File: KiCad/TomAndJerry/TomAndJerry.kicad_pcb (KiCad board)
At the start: 2 copper layers, 1 part

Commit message: Second Test Upload
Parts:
- added REF**: CP_EIA-2012-12_Kemet-R, Capacitor_Tantalum_SMD:CP_EIA-2012-12_Kemet-R, F.Cu at (180.3, 55.9)
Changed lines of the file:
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@@
   )
   (net 0 "")
+  (footprint "Capacitor_Tantalum_SMD:CP_EIA-2012-12_Kemet-R" (layer "F.Cu")
+    (at 180.34 55.88)
+    (descr "Tantalum Capacitor SMD Kemet-R (2012-12 Metric), IPC_7351 nominal, (Body size from: https://www.vishay.com/docs/40182/tmch.pdf), generated with kicad-footprint-generator")
+    (tags "capacitor tantalum")
+    (attr smd)
+    (fp_text reference "REF**" (at 0 -1.58) (layer "F.SilkS")
+      (effects (font (size 1 1) (thickness 0.15)))
+    )
+    (fp_text value "CP_EIA-2012-12_Kemet-R" (at 0 1.58) (layer "F.Fab")
+      (effects (font (size 1 1) (thickness 0.15)))
+    )
+    (fp_text user "${REFERENCE}" (at 0 0) (layer "F.Fab")
+      (effects (font (size 0.5 0.5) (thickness 0.08)))
+    )
+    (fp_line (start -1.71 0.785) (end 1 0.785) (layer "F.SilkS") (width 0.12))
+    (fp_line (start -1.71 -0.785) (end -1.71 0.785) (layer "F.SilkS") (width 0.12))
+    (fp_line (start 1 -0.785) (end -1.71 -0.785) (layer "F.SilkS") (width 0.12))
+    (fp_line (start 1.7 -0.88) (end 1.7 0.88) (layer "F.CrtYd") (width 0.05))
+    (fp_line (start 1.7 0.88) (end -1.7 0.88) (layer "F.CrtYd") (width 0.05))
+    (fp_line (start -1.7 -0.88) (end 1.7 -0.88) (layer "F.CrtYd") (width 0.05))
+    (fp_line (start -1.7 0.88) (end -1.7 -0.88) (layer "F.CrtYd") (width 0.05))
+    (fp_line (start -0.6875 -0.625) (end -1 -0.3125) (layer "F.Fab") (width 0.1))
+    (fp_line (start -1 0.625) (end 1 0.625) (layer "F.Fab") (width 0.1))
+    (fp_line (start 1 0.625) (end 1 -0.625) (layer "F.Fab") (width 0.1))
+    (fp_line (start -1 -0.3125) (end -1 0.625) (layer "F.Fab") (width 0.1))
+    (fp_line (start 1 -0.625) (end -0.6875 -0.625) (layer "F.Fab") (width 0.1))
+    (pad "1" smd roundrect (at -0.8875 0) (size 1.125 1.05) (layers "F.Cu" "F.Paste" "F.Mask") (roundrect_rratio 0.238095))
+    (pad "2" smd roundrect (at 0.8875 0) (size 1.125 1.05) (layers "F.Cu" "F.Paste" "F.Mask") (roundrect_rratio 0.238095))
+    (model "${KICAD6_3DMODEL_DIR}/Capacitor_Tantalum_SMD.3dshapes/CP_EIA-2012-12_Kemet-R.wrl"
+      (offset (xyz 0 0 0))
+      (scale (xyz 1 1 1))
+      (rotate (xyz 0 0 0))
+    )
+  )
   (footprint "Capacitor_Tantalum_SMD:CP_EIA-1608-08_AVX-J" (layer "F.Cu")
     (at 241.3 55.88)

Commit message: 3rd test upload
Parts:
- added REF**: CP_Axial_L10.0mm_D6.0mm_P15.00mm_Horizontal, Capacitor_THT:CP_Axial_L10.0mm_D6.0mm_P15.00mm_Horizontal, F.Cu at (205.7, 48.3)
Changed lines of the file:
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@@
+    )
+  )
+  (footprint "Capacitor_THT:CP_Axial_L10.0mm_D6.0mm_P15.00mm_Horizontal" (layer "F.Cu")
+    (at 205.74 48.26)
+    (descr "CP, Axial series, Axial, Horizontal, pin pitch=15mm, , length*diameter=10*6mm^2, Electrolytic Capacitor, , http://www.vishay.com/docs/28325/021asm.pdf")
+    (tags "CP Axial series Axial Horizontal pin pitch 15mm  length 10mm diameter 6mm Electrolytic Capacitor")
+    (attr through_hole)
+    (fp_text reference "REF**" (at 7.5 -4.12) (layer "F.SilkS")
+      (effects (font (size 1 1) (thickness 0.15)))
+    )
+    (fp_text value "CP_Axial_L10.0mm_D6.0mm_P15.00mm_Horizontal" (at 7.5 4.12) (layer "F.Fab")
+      (effects (font (size 1 1) (thickness 0.15)))
+    )
+    (fp_text user "${REFERENCE}" (at 7.5 0) (layer "F.Fab")
+      (effects (font (size 1 1) (thickness 0.15)))
+    )
+    (fp_line (start 3.88 -3.12) (end 4.63 -2.37) (layer "F.SilkS") (width 0.12))
+    (fp_line (start 13.76 0) (end 12.62 0) (layer "F.SilkS") (width 0.12))
+    (fp_line (start 1.24 0) (end 2.38 0) (layer "F.SilkS") (width 0.12))
+    (fp_line (start 0.63 -2.2) (end 2.13 -2.2) (layer "F.SilkS") (width 0.12))
+    (fp_line (start 3.88 3.12) (end 4.63 2.37) (layer "F.SilkS") (width 0.12))
+    (fp_line (start 4.63 2.37) (end 5.38 3.12) (layer "F.SilkS") (width 0.12))
+    (fp_line (start 12.62 -3.12) (end 12.62 3.12) (layer "F.SilkS") (width 0.12))
+    (fp_line (start 1.38 -2.95) (end 1.38 -1.45) (layer "F.SilkS") (width 0.12))
+    (fp_line (start 2.38 -3.12) (end 3.88 -3.12) (layer "F.SilkS") (width 0.12))
+    (fp_line (start 2.38 -3.12) (end 2.38 3.12) (layer "F.SilkS") (width 0.12))
+    (fp_line (start 5.38 3.12) (end 12.62 3.12) (layer "F.SilkS") (width 0.12))
+    (fp_line (start 4.63 -2.37) (end 5.38 -3.12) (layer "F.SilkS") (width 0.12))
+    (fp_line (start 5.38 -3.12) (end 12.62 -3.12) (layer "F.SilkS") (width 0.12))
+    (fp_line (start 2.38 3.12) (end 3.88 3.12) (layer "F.SilkS") (width 0.12))
+    (fp_line (start 16.25 3.25) (end 16.25 -3.25) (layer "F.CrtYd") (width 0.05))
+    (fp_line (start -1.25 3.25) (end 16.25 3.25) (layer "F.CrtYd") (width 0.05))
+    (fp_line (start 16.25 -3.25) (end -1.25 -3.25) (layer "F.CrtYd") (width 0.05))
+    (fp_line (start -1.25 -3.25) (end -1.25 3.25) (layer "F.CrtYd") (width 0.05))
+    (fp_line (start 3.88 -3) (end 4.63 -2.25) (layer "F.Fab") (width 0.1))
+    (fp_line (start 3.88 3) (end 4.63 2.25) (layer "F.Fab") (width 0.1))
+    (fp_line (start 2.5 3) (end 3.88 3) (layer "F.Fab") (width 0.1))
+    (fp_line (start 2.5 -3) (end 3.88 -3) (layer "F.Fab") (width 0.1))
+    (fp_line (start 4.63 -2.25) (end 5.38 -3) (layer "F.Fab") (width 0.1))
+    (fp_line (start 5.38 3) (end 12.5 3) (layer "F.Fab") (width 0.1))
+    (fp_line (start 5.38 -3) (end 12.5 -3) (layer "F.Fab") (width 0.1))
+    (fp_line (start 12.5 -3) (end 12.5 3) (layer "F.Fab") (width 0.1))
+    (fp_line (start 2.5 -3) (end 2.5 3) (layer "F.Fab") (width 0.1))
+    (fp_line (start 3.9 0) (end 5.4 0) (layer "F.Fab") (width 0.1))
+    (fp_line (start 4.63 2.25) (end 5.38 3) (layer "F.Fab") (width 0.1))
+    (fp_line (start 4.65 -0.75) (end 4.65 0.75) (layer "F.Fab") (width 0.1))
+    (fp_line (start 0 0) (end 2.5 0) (layer "F.Fab") (width 0.1))
+    (fp_line (start 15 0) (end 12.5 0) (layer "F.Fab") (width 0.1))
+    (pad "1" thru_hole rect (at 0 0) (size 2 2) (drill 1) (layers *.Cu *.Mask))
+    (pad "2" thru_hole oval (at 15 0) (size 2 2) (drill 1) (layers *.Cu *.Mask))
+    (model "${KICAD6_3DMODEL_DIR}/Capacitor_THT.3dshapes/CP_Axial_L10.0mm_D6.0mm_P15.00mm_Horizontal.wrl"
+      (offset (xyz 0 0 0))
+      (scale (xyz 1 1 1))
+      (rotate (xyz 0 0 0))
     )
   )

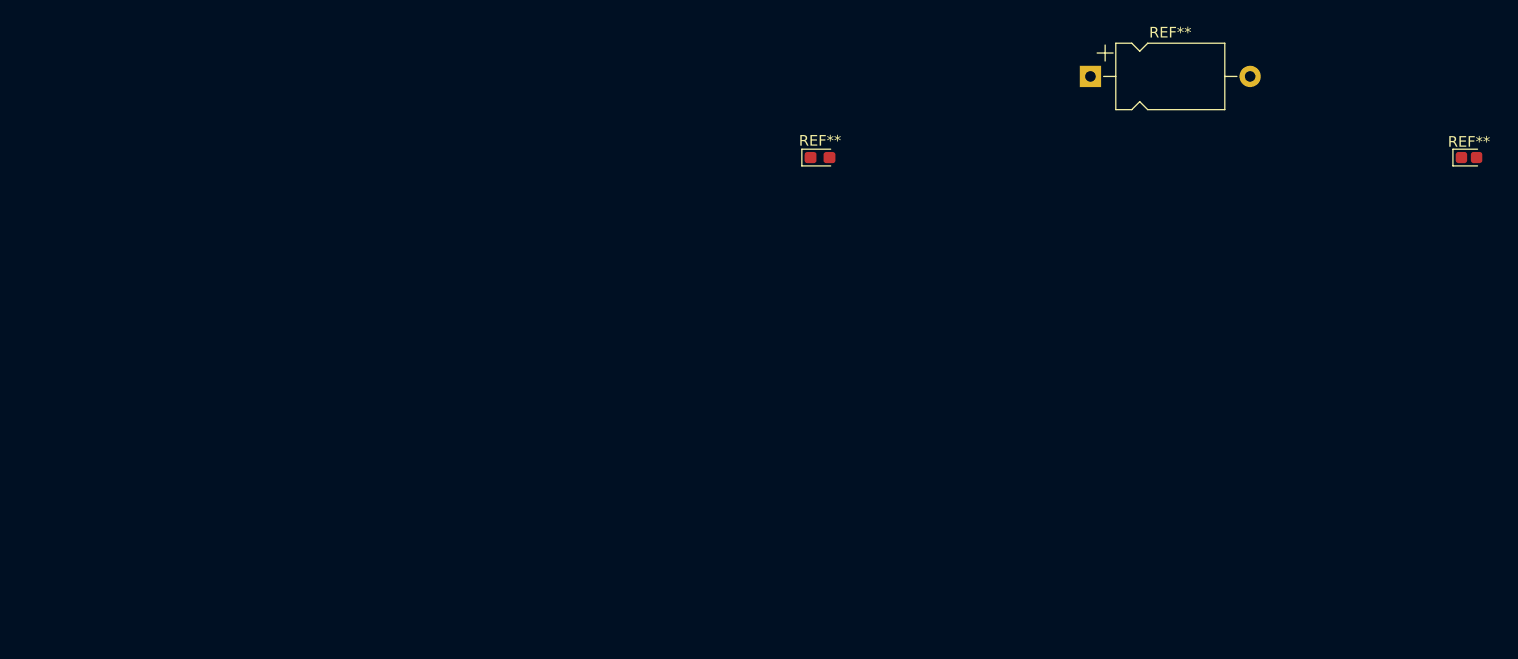
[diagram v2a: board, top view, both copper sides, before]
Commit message: Beginning of visualizing Parts (uncommitted from 2/2/22)
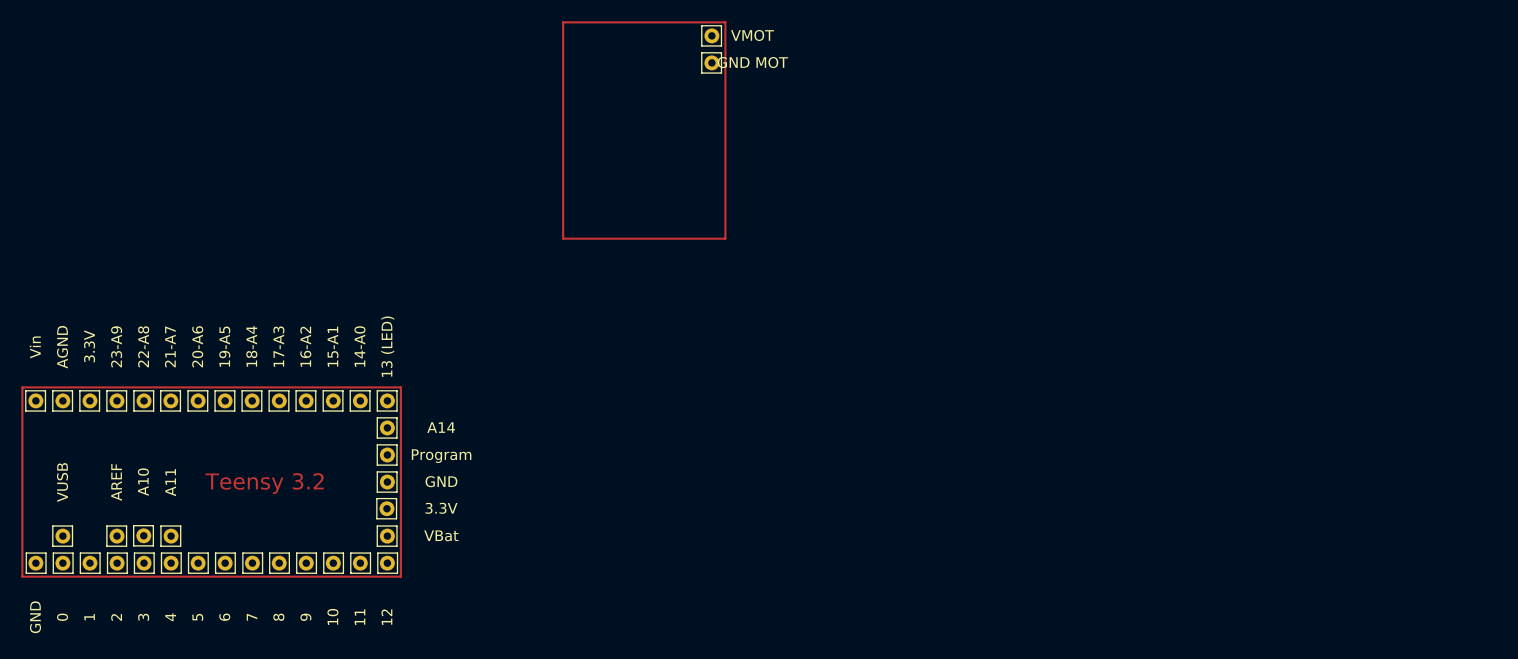
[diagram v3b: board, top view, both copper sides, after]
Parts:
- removed REF**: CP_EIA-2012-12_Kemet-R, Capacitor_Tantalum_SMD:CP_EIA-2012-12_Kemet-R
- removed REF**: CP_Axial_L10.0mm_D6.0mm_P15.00mm_Horizontal, Capacitor_THT:CP_Axial_L10.0mm_D6.0mm_P15.00mm_Horizontal
- removed REF**: CP_EIA-1608-08_AVX-J, Capacitor_Tantalum_SMD:CP_EIA-1608-08_AVX-J
- added 0: Pin_D0.7mm_L6.5mm_W1.8mm_FlatFork, Connector_Pin:Pin_D0.7mm_L6.5mm_W1.8mm_FlatFork, F.Cu at (109.2, 94.0)
- added 1: Pin_D0.7mm_L6.5mm_W1.8mm_FlatFork, Connector_Pin:Pin_D0.7mm_L6.5mm_W1.8mm_FlatFork, F.Cu at (111.8, 94.0)
- added 10: Pin_D0.7mm_L6.5mm_W1.8mm_FlatFork, Connector_Pin:Pin_D0.7mm_L6.5mm_W1.8mm_FlatFork, F.Cu at (134.6, 94.0)
- added 11: Pin_D0.7mm_L6.5mm_W1.8mm_FlatFork, Connector_Pin:Pin_D0.7mm_L6.5mm_W1.8mm_FlatFork, F.Cu at (137.2, 94.0)
- added 12: Pin_D0.7mm_L6.5mm_W1.8mm_FlatFork, Connector_Pin:Pin_D0.7mm_L6.5mm_W1.8mm_FlatFork, F.Cu at (139.7, 94.0)
- added 13 (LED): Pin_D0.7mm_L6.5mm_W1.8mm_FlatFork, Connector_Pin:Pin_D0.7mm_L6.5mm_W1.8mm_FlatFork, F.Cu at (139.7, 78.7)
- added 14-A0: Pin_D0.7mm_L6.5mm_W1.8mm_FlatFork, Connector_Pin:Pin_D0.7mm_L6.5mm_W1.8mm_FlatFork, F.Cu at (137.2, 78.7)
- added 15-A1: Pin_D0.7mm_L6.5mm_W1.8mm_FlatFork, Connector_Pin:Pin_D0.7mm_L6.5mm_W1.8mm_FlatFork, F.Cu at (134.6, 78.7)
- added 16-A2: Pin_D0.7mm_L6.5mm_W1.8mm_FlatFork, Connector_Pin:Pin_D0.7mm_L6.5mm_W1.8mm_FlatFork, F.Cu at (132.1, 78.7)
- added 17-A3: Pin_D0.7mm_L6.5mm_W1.8mm_FlatFork, Connector_Pin:Pin_D0.7mm_L6.5mm_W1.8mm_FlatFork, F.Cu at (129.5, 78.7)
- added 18-A4: Pin_D0.7mm_L6.5mm_W1.8mm_FlatFork, Connector_Pin:Pin_D0.7mm_L6.5mm_W1.8mm_FlatFork, F.Cu at (127.0, 78.7)
- added 19-A5: Pin_D0.7mm_L6.5mm_W1.8mm_FlatFork, Connector_Pin:Pin_D0.7mm_L6.5mm_W1.8mm_FlatFork, F.Cu at (124.5, 78.7)
- added 2: Pin_D0.7mm_L6.5mm_W1.8mm_FlatFork, Connector_Pin:Pin_D0.7mm_L6.5mm_W1.8mm_FlatFork, F.Cu at (114.3, 94.0)
- added 20-A6: Pin_D0.7mm_L6.5mm_W1.8mm_FlatFork, Connector_Pin:Pin_D0.7mm_L6.5mm_W1.8mm_FlatFork, F.Cu at (121.9, 78.7)
- added 21-A7: Pin_D0.7mm_L6.5mm_W1.8mm_FlatFork, Connector_Pin:Pin_D0.7mm_L6.5mm_W1.8mm_FlatFork, F.Cu at (119.4, 78.7)
- added 22-A8: Pin_D0.7mm_L6.5mm_W1.8mm_FlatFork, Connector_Pin:Pin_D0.7mm_L6.5mm_W1.8mm_FlatFork, F.Cu at (116.8, 78.7)
- added 23-A9: Pin_D0.7mm_L6.5mm_W1.8mm_FlatFork, Connector_Pin:Pin_D0.7mm_L6.5mm_W1.8mm_FlatFork, F.Cu at (114.3, 78.7)
- added 3: Pin_D0.7mm_L6.5mm_W1.8mm_FlatFork, Connector_Pin:Pin_D0.7mm_L6.5mm_W1.8mm_FlatFork, F.Cu at (116.8, 94.0)
- added 3.3V: Pin_D0.7mm_L6.5mm_W1.8mm_FlatFork, Connector_Pin:Pin_D0.7mm_L6.5mm_W1.8mm_FlatFork, F.Cu at (139.7, 88.9)
- added 3.3V: Pin_D0.7mm_L6.5mm_W1.8mm_FlatFork, Connector_Pin:Pin_D0.7mm_L6.5mm_W1.8mm_FlatFork, F.Cu at (111.8, 78.7)
- added 4: Pin_D0.7mm_L6.5mm_W1.8mm_FlatFork, Connector_Pin:Pin_D0.7mm_L6.5mm_W1.8mm_FlatFork, F.Cu at (119.4, 94.0)
- added 5: Pin_D0.7mm_L6.5mm_W1.8mm_FlatFork, Connector_Pin:Pin_D0.7mm_L6.5mm_W1.8mm_FlatFork, F.Cu at (121.9, 94.0)
- added 6: Pin_D0.7mm_L6.5mm_W1.8mm_FlatFork, Connector_Pin:Pin_D0.7mm_L6.5mm_W1.8mm_FlatFork, F.Cu at (124.5, 94.0)
- added 7: Pin_D0.7mm_L6.5mm_W1.8mm_FlatFork, Connector_Pin:Pin_D0.7mm_L6.5mm_W1.8mm_FlatFork, F.Cu at (127.0, 94.0)
- added 8: Pin_D0.7mm_L6.5mm_W1.8mm_FlatFork, Connector_Pin:Pin_D0.7mm_L6.5mm_W1.8mm_FlatFork, F.Cu at (129.5, 94.0)
- added 9: Pin_D0.7mm_L6.5mm_W1.8mm_FlatFork, Connector_Pin:Pin_D0.7mm_L6.5mm_W1.8mm_FlatFork, F.Cu at (132.1, 94.0)
- added A10: Pin_D0.7mm_L6.5mm_W1.8mm_FlatFork, Connector_Pin:Pin_D0.7mm_L6.5mm_W1.8mm_FlatFork, F.Cu at (116.8, 91.4)
- added A11: Pin_D0.7mm_L6.5mm_W1.8mm_FlatFork, Connector_Pin:Pin_D0.7mm_L6.5mm_W1.8mm_FlatFork, F.Cu at (119.4, 91.4)
- added A14: Pin_D0.7mm_L6.5mm_W1.8mm_FlatFork, Connector_Pin:Pin_D0.7mm_L6.5mm_W1.8mm_FlatFork, F.Cu at (139.7, 81.3)
- added AGND: Pin_D0.7mm_L6.5mm_W1.8mm_FlatFork, Connector_Pin:Pin_D0.7mm_L6.5mm_W1.8mm_FlatFork, F.Cu at (109.2, 78.7)
- added AREF: Pin_D0.7mm_L6.5mm_W1.8mm_FlatFork, Connector_Pin:Pin_D0.7mm_L6.5mm_W1.8mm_FlatFork, F.Cu at (114.3, 91.4)
- added GND: Pin_D0.7mm_L6.5mm_W1.8mm_FlatFork, Connector_Pin:Pin_D0.7mm_L6.5mm_W1.8mm_FlatFork, F.Cu at (106.7, 94.0)
- added GND MOT: Pin_D0.7mm_L6.5mm_W1.8mm_FlatFork, Connector_Pin:Pin_D0.7mm_L6.5mm_W1.8mm_FlatFork, F.Cu at (170.2, 47.0)
- added GND: Pin_D0.7mm_L6.5mm_W1.8mm_FlatFork, Connector_Pin:Pin_D0.7mm_L6.5mm_W1.8mm_FlatFork, F.Cu at (139.7, 86.4)
- added Program: Pin_D0.7mm_L6.5mm_W1.8mm_FlatFork, Connector_Pin:Pin_D0.7mm_L6.5mm_W1.8mm_FlatFork, F.Cu at (139.7, 83.8)
- added VBat: Pin_D0.7mm_L6.5mm_W1.8mm_FlatFork, Connector_Pin:Pin_D0.7mm_L6.5mm_W1.8mm_FlatFork, F.Cu at (139.7, 91.4)
- added VMOT: Pin_D0.7mm_L6.5mm_W1.8mm_FlatFork, Connector_Pin:Pin_D0.7mm_L6.5mm_W1.8mm_FlatFork, F.Cu at (170.2, 44.5)
- added VUSB: Pin_D0.7mm_L6.5mm_W1.8mm_FlatFork, Connector_Pin:Pin_D0.7mm_L6.5mm_W1.8mm_FlatFork, F.Cu at (109.2, 91.4)
- added Vin: Pin_D0.7mm_L6.5mm_W1.8mm_FlatFork, Connector_Pin:Pin_D0.7mm_L6.5mm_W1.8mm_FlatFork, F.Cu at (106.7, 78.7)
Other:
- board text added: "Teensy 3.2"
